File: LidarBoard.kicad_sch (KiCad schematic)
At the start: 33 parts, among them J21 USB_C_Receptacle_USB2.0_16P, J22 to TopBoard, J23 LIDAR, J24 ST-Link, Q8 BSS138, SW10 MODE_SWITCH, SW11 TC-06104-043E, SW12 TC-06104-043E, SW9 RESET_SWITCH, U17 RT9080-33GJ5, U18 Sit2001B, U19 STM32F446RET6

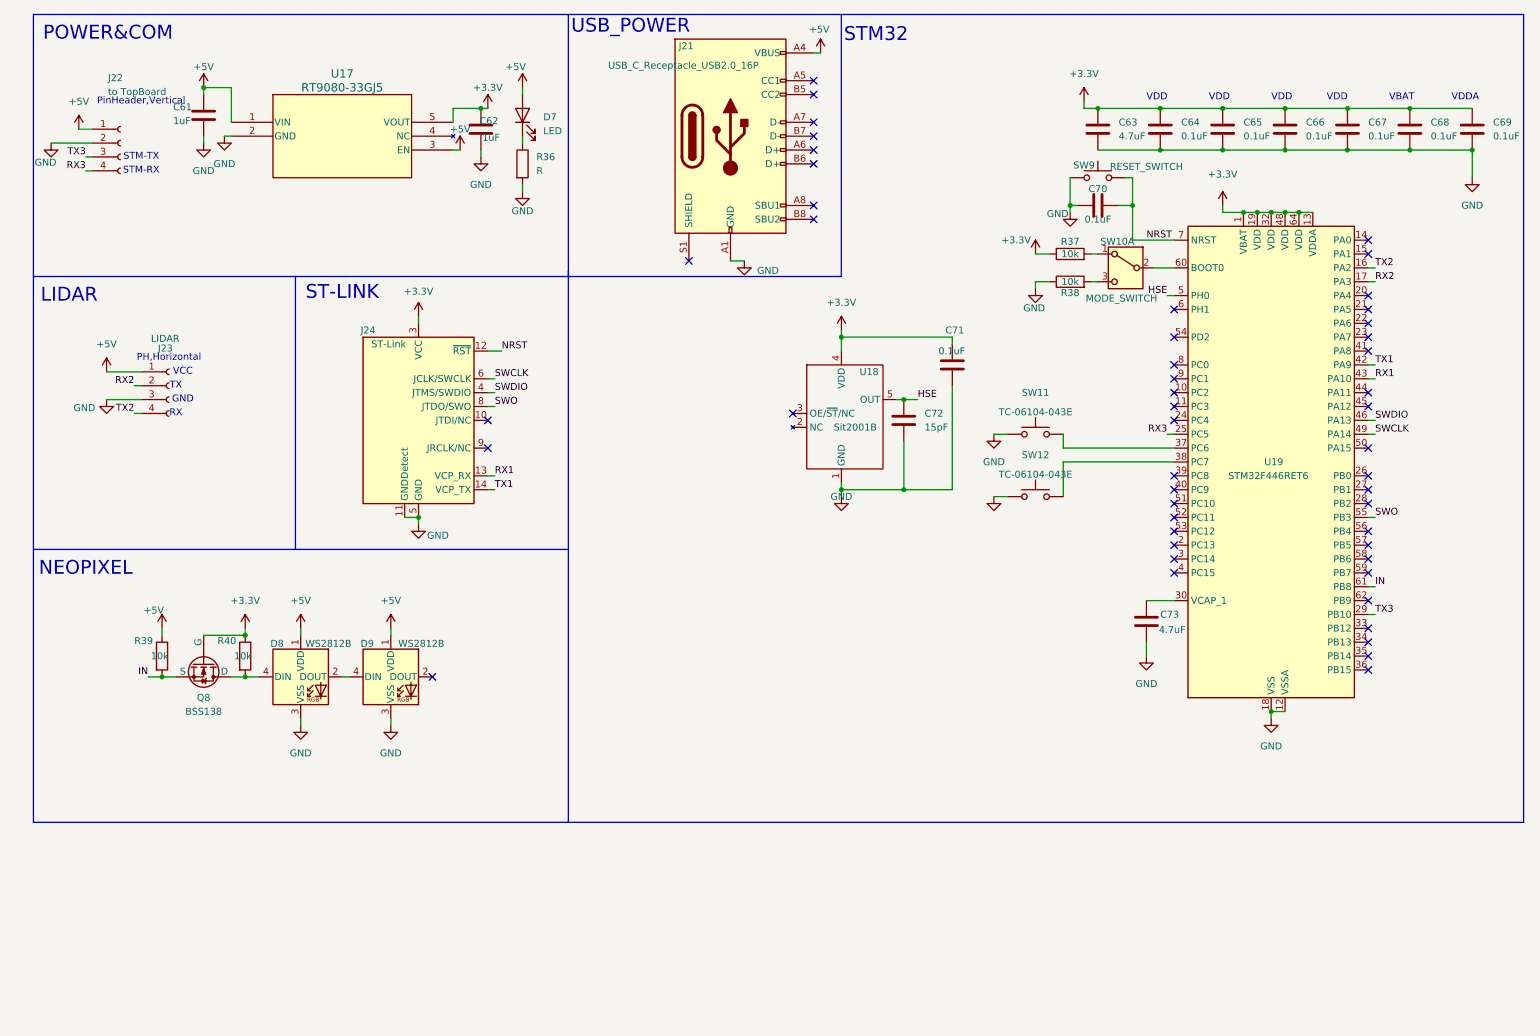
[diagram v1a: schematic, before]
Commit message: Lidar基板Rev.2発注
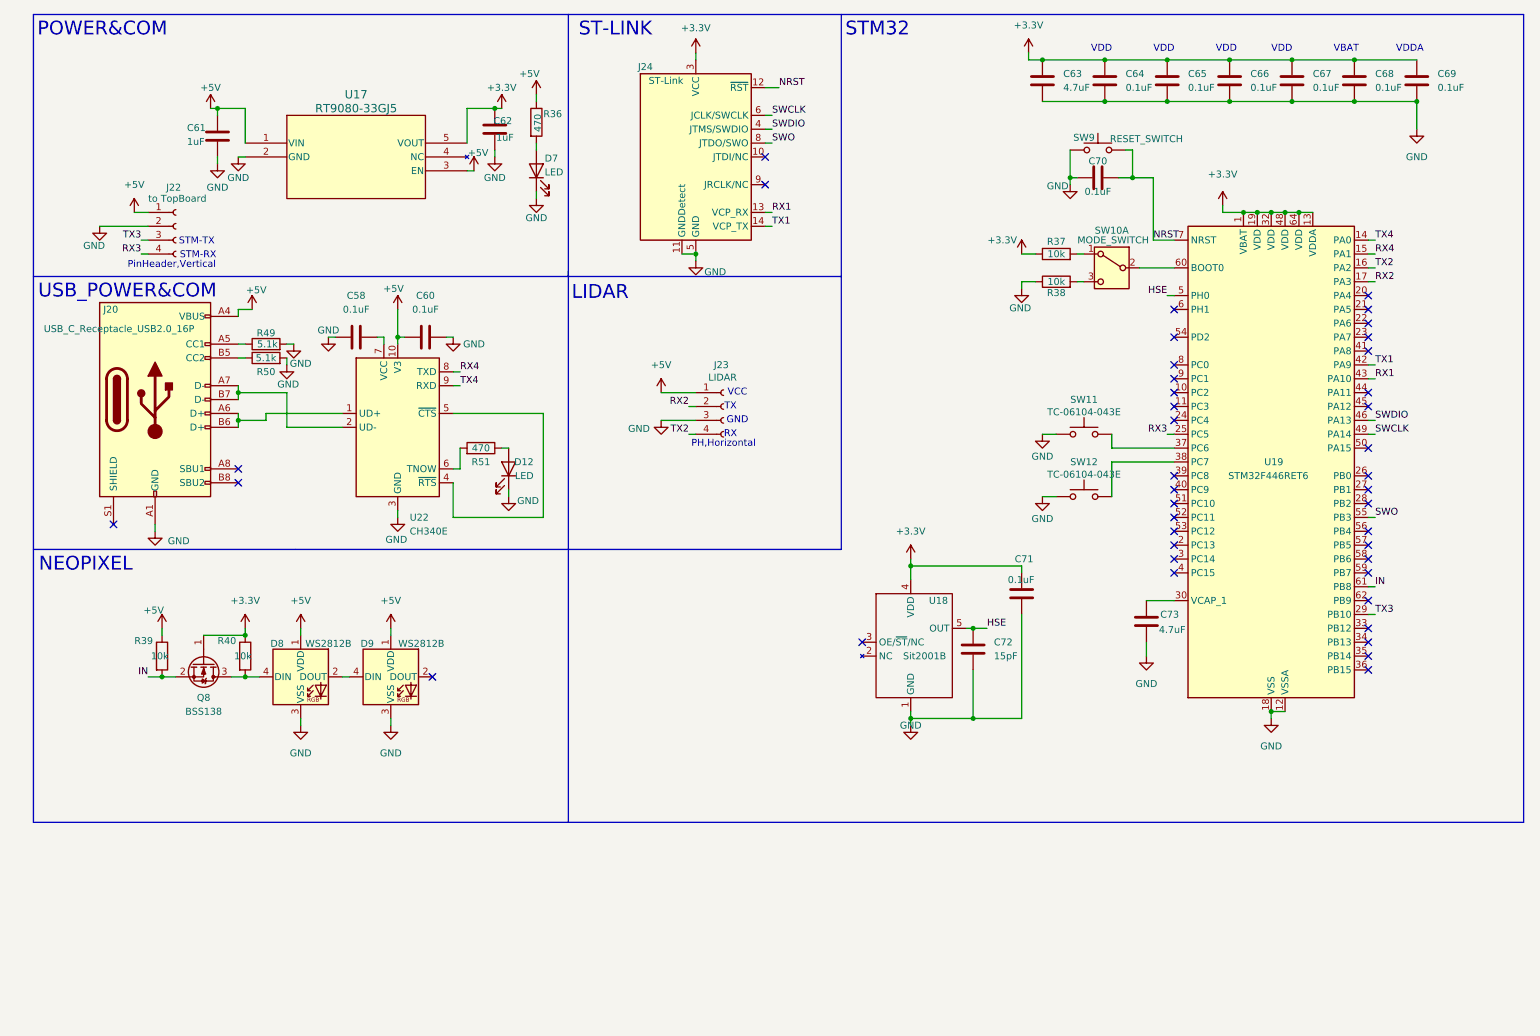
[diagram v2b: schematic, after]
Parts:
- removed J21: USB_C_Receptacle_USB2.0_16P, Connector_USB:USB_C_Receptacle_G-Switch_GT-USB-7010ASV, symbol Connector:USB_C_Receptacle_USB2.0_16P
- removed Q8: BSS138, Package_TO_SOT_SMD:SOT-23, symbol Simulation_SPICE:NMOS
- added C58, C60: 0.1uF, Capacitor_SMD:C_0603_1608Metric, symbol Device:C
- added D12: LED, LED_SMD:LED_0603_1608Metric, symbol Device:LED
- added J20: USB_C_Receptacle_USB2.0_16P, Connector_USB:USB_C_Receptacle_G-Switch_GT-USB-7010ASV, symbol Connector:USB_C_Receptacle_USB2.0_16P
- added Q8: BSS138, Package_TO_SOT_SMD:SOT-23, symbol Transistor_FET:BSS138
- added R49, R50: 5.1k, Resistor_SMD:R_0603_1608Metric, symbol Device:R
- added R51: 470, Resistor_SMD:R_0603_1608Metric, symbol Device:R
- added U22: CH340E, Package_SO:MSOP-10_3x3mm_P0.5mm, symbol Interface_USB:CH340E
- C61, C62, C63, C64, C65, C66, C67, C68, C69, C70, C71, C72, C73: footprint Capacitor_SMD:C_0402_1005Metric -> Capacitor_SMD:C_0603_1608Metric
- D7: footprint Diode_SMD:D_0603_1608Metric -> LED_SMD:LED_0603_1608Metric
- R36: value R -> 470; footprint Capacitor_SMD:C_0402_1005Metric -> Resistor_SMD:R_0603_1608Metric
- R37, R38, R39, R40: footprint Capacitor_SMD:C_0402_1005Metric -> Resistor_SMD:R_0603_1608Metric
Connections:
- net +3.3V: now also Q8.1 (G)
- net +5V: now also R36.1, C60.1, J20.A4 (VBUS), J20.A9 (VBUS), J20.B4 (VBUS), J20.B9 (VBUS), U22.10 (V3); no longer D7.2 (A)
- net GND: now also D7.1 (K), C58.1, C60.2, D12.1 (K), J20.A1 (GND), J20.A12 (GND), J20.B1 (GND), J20.B12 (GND), R49.2, R50.2, U22.3 (GND); no longer R36.2
- net IN: now also Q8.2 (S)
- net at D8.4 (DIN), R40.2: now also Q8.3 (D)
- net TX4: now reaches U19.14 (PA0)
- net TX4: now also U22.9 (RXD)
- net RX4: now reaches U19.15 (PA1)
- net RX4: now also U22.8 (TXD)
- new net: J20.B5 (CC2), R50.1
- new net: D12.2 (A), R51.1
- new net: C58.2, U22.7 (VCC)
- new net: J20.A5 (CC1), R49.1
- new net: D7.2 (A), R36.2
- new net: R51.2, U22.6 (TNOW)
- new net: J20.A6 (D+), J20.B6 (D+), U22.1 (UD+)
- new net: J20.A7 (D-), J20.B7 (D-), U22.2 (UD-)
- new net: U22.4 (~{RTS}), U22.5 (~{CTS})
- no-connect marks 50 -> 42
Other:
- note added: "USB_POWER&COM"
- note removed: "USB_POWER"
- company: (none) -> Fornax
- title: (none) -> LidarBoard Rev.2
- moved on the sheet: C61, C62, C63, C64, C65, C66, C67, C68, C69, C70, C71, C72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

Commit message: LiDAR基板Rev.2修正
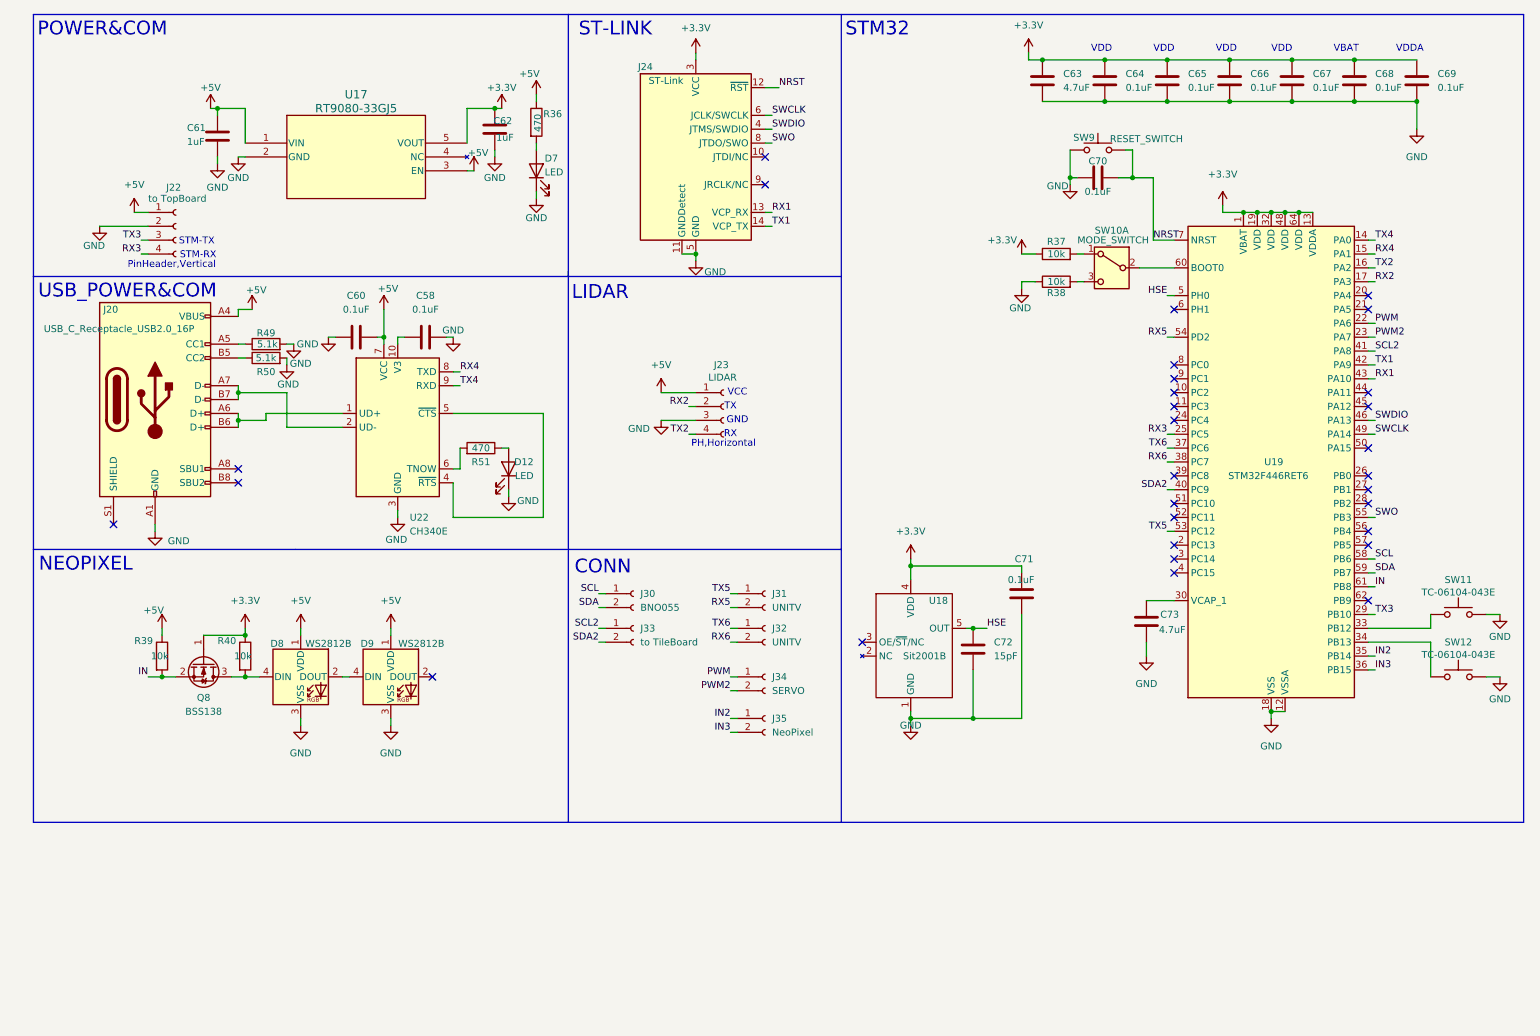
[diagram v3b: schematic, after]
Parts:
- added J30: BNO055, Connector_PinSocket_1.27mm:PinSocket_1x02_P1.27mm_Vertical, symbol Connector:Conn_01x02_Socket
- added J31, J32: UNITV, Connector_PinSocket_1.27mm:PinSocket_1x02_P1.27mm_Vertical, symbol Connector:Conn_01x02_Socket
- added J33: to TileBoard, Connector_PinSocket_1.27mm:PinSocket_1x02_P1.27mm_Vertical, symbol Connector:Conn_01x02_Socket
- added J34: SERVO, Connector_PinSocket_1.27mm:PinSocket_1x02_P1.27mm_Vertical, symbol Connector:Conn_01x02_Socket
- added J35: NeoPixel, Connector_PinSocket_1.27mm:PinSocket_1x02_P1.27mm_Vertical, symbol Connector:Conn_01x02_Socket
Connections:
- net +5V: now also U22.7 (VCC); no longer U22.10 (V3)
- net PWM: now reaches U19.22 (PA6)
- net PWM: now also J34.1 (Pin_1)
- net PWM2: now reaches U19.23 (PA7)
- net PWM2: now also J34.2 (Pin_2)
- net at U19.33 (PB12): now also SW11.2
- net at U19.34 (PB13): now also SW12.2
- net IN2: now reaches U19.35 (PB14)
- net IN2: now also J35.1 (Pin_1)
- net IN3: now reaches U19.36 (PB15)
- net IN3: now also J35.2 (Pin_2)
- net TX6: now reaches U19.37 (PC6)
- net TX6: now also J32.1 (Pin_1); no longer SW11.2
- net RX6: now reaches U19.38 (PC7)
- net RX6: now also J32.2 (Pin_2); no longer SW12.2
- net SDA2: now reaches U19.40 (PC9)
- net SDA2: now also J33.2 (Pin_2)
- net SCL2: now reaches U19.41 (PA8)
- net SCL2: now also J33.1 (Pin_1)
- net TX5: now reaches U19.53 (PC12)
- net TX5: now also J31.1 (Pin_1)
- net RX5: now reaches U19.54 (PD2)
- net RX5: now also J31.2 (Pin_2)
- net SCL: now reaches U19.58 (PB6)
- net SCL: now also J30.1 (Pin_1)
- net SDA: now reaches U19.59 (PB7)
- net SDA: now also J30.2 (Pin_2)
- net at C58.2: now also U22.10 (V3); no longer U22.7 (VCC)
- no-connect marks 42 -> 30
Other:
- note added: "CONN"

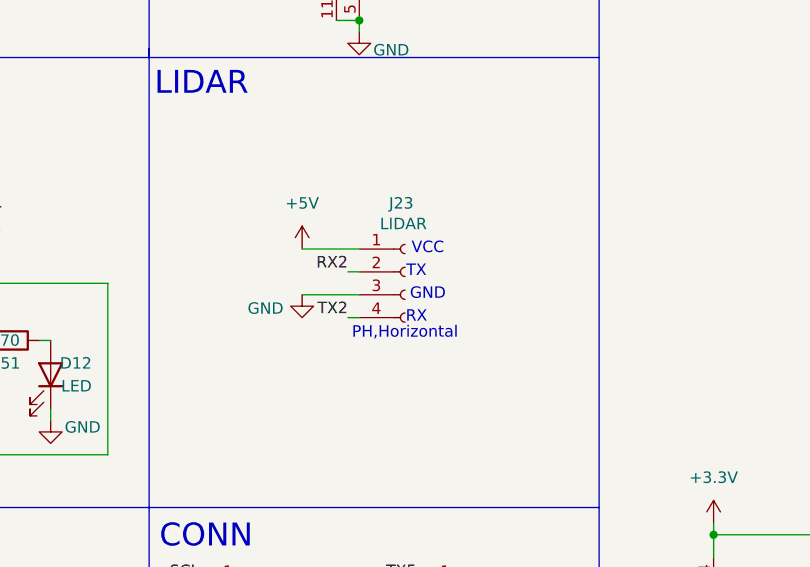
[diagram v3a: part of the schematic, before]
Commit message: LiDAR基板Rev.2修正v2
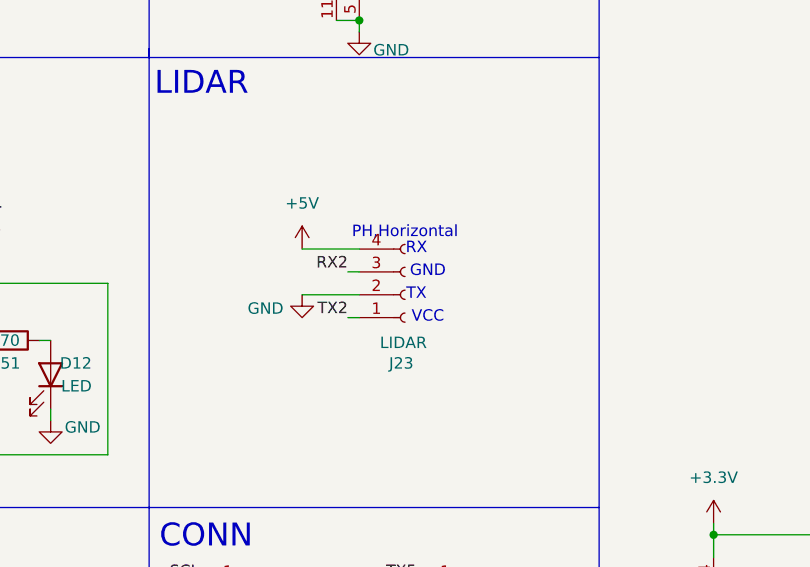
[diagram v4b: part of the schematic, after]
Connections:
- net +5V: now also J23.4 (Pin_4); no longer J23.1 (Pin_1)
- net GND: now also J23.2 (Pin_2); no longer J23.3 (Pin_3)
- net RX2: now also J23.3 (Pin_3); no longer J23.2 (Pin_2)
- net TX2: now also J23.1 (Pin_1); no longer J23.4 (Pin_4)
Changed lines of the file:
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@@
 		)
 	)
-	(text "VDD"
+	(text "TX"
 		(exclude_from_sim no)
-		(at 238.76 19.05 0)
+		(at 139.7 86.36 0)
 		(effects
 			(font
 				(size 1.27 1.27)
 			)
-			(justify left bottom)
 		)
 	)
 	(text "VDD"
 		(exclude_from_sim no)
-		(at 217.17 19.05 0)
+		(at 238.76 19.05 0)
 		(effects
 			(font
@@
 		)
 	)
-	(text "TX"
+	(text "VDD"
 		(exclude_from_sim no)
-		(at 139.7 83.82 0)
+		(at 217.17 19.05 0)
 		(effects
 			(font
 				(size 1.27 1.27)
 			)
+			(justify left bottom)
 		)
 	)
@@
 		)
 	)
-	(text "GND"
+	(text "RX"
 		(exclude_from_sim no)
-		(at 140.97 86.36 0)
+		(at 139.7 81.28 0)
 		(effects
 			(font
@@
 	(text "VCC"
 		(exclude_from_sim no)
-		(at 140.97 81.28 0)
+		(at 140.97 88.9 0)
 		(effects
 			(font
@@
 		)
 	)
-	(text "RX"
+	(text "VDD"
 		(exclude_from_sim no)
-		(at 139.7 88.9 0)
+		(at 228.6 19.05 0)
 		(effects
 			(font
 				(size 1.27 1.27)
 			)
+			(justify left bottom)
 		)
 	)
-	(text "VDD"
+	(text "STM32"
 		(exclude_from_sim no)
-		(at 228.6 19.05 0)
+		(at 166.624 14.732 0)
 		(effects
 			(font
-				(size 1.27 1.27)
+				(size 2.54 2.54)
 			)
-			(justify left bottom)
 		)
 	)
-	(text "STM32"
+	(text "CONN"
 		(exclude_from_sim no)
-		(at 166.624 14.732 0)
+		(at 116.332 113.284 0)
 		(effects
 			(font
@@
 	(text "PH,Horizontal"
 		(exclude_from_sim no)
-		(at 138.43 90.678 0)
+		(at 138.43 79.502 0)
 		(effects
 			(font
@@
 		)
 	)
-	(text "CONN"
+	(text "POWER&COM"
 		(exclude_from_sim no)
-		(at 116.332 113.284 0)
+		(at 24.638 14.732 0)
 		(effects
 			(font
@@
 		)
 	)
-	(text "POWER&COM"
+	(text "GND"
 		(exclude_from_sim no)
-		(at 24.638 14.732 0)
+		(at 140.97 83.82 0)
 		(effects
 			(font
-				(size 2.54 2.54)
+				(size 1.27 1.27)
 			)
 		)
@@
 	)
 	(symbol
-		(lib_id "Connector:Conn_01x04_Socket")
-		(at 138.43 83.82 0)
-		(unit 1)
-		(exclude_from_sim no)
-		(in_bom yes)
-		(on_board yes)
-		(dnp no)
-		(property "Reference" "J23"
-			(at 136.652 76.2 0)
-			(effects
-				(font
-					(size 1.27 1.27)
-				)
-				(justify left)
-			)
-		)
-		(property "Value" "LIDAR"
-			(at 135.636 78.486 0)
-			(effects
-				(font
-					(size 1.27 1.27)
-				)
-				(justify left)
-			)
-		)
-		(property "Footprint" "Connector_JST:JST_PH_S4B-PH-K_1x04_P2.00mm_Horizontal"
-			(at 138.43 83.82 0)
-			(effects
-				(font
-					(size 1.27 1.27)
-				)
-				(hide yes)
-			)
-		)
-		(property "Datasheet" "~"
-			(at 138.43 83.82 0)
-			(effects
-				(font
-					(size 1.27 1.27)
-				)
-				(hide yes)
-			)
-		)
-		(property "Description" "Generic connector, single row, 01x04, script generated"
-			(at 138.43 83.82 0)
-			(effects
-				(font
-					(size 1.27 1.27)
-				)
-				(hide yes)
-			)
-		)
-		(pin "1"
-		)
-		(pin "3"
-		)
-		(pin "4"
-		)
-		(pin "2"
-		)
-		(instances
-			(project ""
-				(path "/af3cfa74-a4e1-440c-b447-a23ba1001a82/420fe028-99c2-46f7-82ef-d02bfa595c0b"
-					(reference "J23")
-					(unit 1)
-				)
-			)
-		)
-	)
-	(symbol
 		(lib_id "power:+3.3V")
 		(at 193.04 55.88 0)
@@
 					(unit 1)
 				)
+			)
+		)
+	)
+	(symbol
+		(lib_id "Connector:Conn_01x04_Socket")
+		(at 138.43 86.36 0)
+		(mirror x)
+		(unit 1)
+		(exclude_from_sim no)
+		(in_bom yes)
+		(on_board yes)
+		(dnp no)
+		(property "Reference" "J23"
+			(at 136.652 93.98 0)
+			(effects
+				(font
+					(size 1.27 1.27)
+				)
+				(justify left)
+			)
+		)
+		(property "Value" "LIDAR"
+			(at 135.636 91.694 0)
+			(effects
+				(font
+					(size 1.27 1.27)
+				)
+				(justify left)
+			)
+		)
+		(property "Footprint" "Connector_JST:JST_PH_S4B-PH-K_1x04_P2.00mm_Horizontal"
+			(at 138.43 86.36 0)
+			(effects
+				(font
+					(size 1.27 1.27)
+				)
+				(hide yes)
+			)
+		)
+		(property "Datasheet" "~"
+			(at 138.43 86.36 0)
+			(effects
+				(font
+					(size 1.27 1.27)
+				)
+				(hide yes)
+			)
+		)
+		(property "Description" "Generic connector, single row, 01x04, script generated"
+			(at 138.43 86.36 0)
+			(effects
+				(font
+					(size 1.27 1.27)
+				)
+				(hide yes)
+			)
+		)
+		(pin "1"
+		)
+		(pin "3"
+		)
+		(pin "4"
+		)
+		(pin "2"
+		)
+		(instances
+			(project "Rev.1"
+				(path "/af3cfa74-a4e1-440c-b447-a23ba1001a82/420fe028-99c2-46f7-82ef-d02bfa595c0b"
+					(reference "J23")
+					(unit 1)
+				)

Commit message: メイン基板Rev.2完成
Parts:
- removed J23: LIDAR, Connector_JST:JST_PH_S4B-PH-K_1x04_P2.00mm_Horizontal, symbol Connector:Conn_01x04_Socket
- added J22: LIDAR, Connector_JST:JST_PH_S4B-PH-K_1x04_P2.00mm_Horizontal, symbol Connector:Conn_01x04_Socket
- renumbered C63 to C49, C64 to C50, C65 to C51, C66 to C52, C67 to C53, C68 to C54, C69 to C55, C62 to C56, C61 to C57, C70 to C58, C60 to C59, C58 to C60, C71 to C61, C73 to C62, C72 to C63, D8 to D10, D9 to D11, D7 to D8, D12 to D9, J24 to J19, J22 to J20, J20 to J21, J30 to J23, J31 to J24, J33 to J25, J32 to J26, J34 to J27, J35 to J28, Q8 to Q6, R36 to R35, R37 to R36, R38 to R37, R49 to R38, R50 to R39, R51 to R40, R39 to R41, R40 to R42, U17 to U19, U22 to U20, U19 to U21, U18 to U22
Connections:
- net +5V: now also J22.1 (Pin_1)
- net GND: now also J22.3 (Pin_3)
- net RX2: now also J22.2 (Pin_2)
- net TX2: now also J22.4 (Pin_4)
